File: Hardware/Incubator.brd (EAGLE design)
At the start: 50 x 50 mm, 41 parts, among them IC1 STM32F050F, IC2 LD117AS33TR, IC3 7805DT, Q1 8 MHz, Q2 BC817-16LT1SMD, U1 LCD-16X28X2, X1 22-23-2051, X2 22-23-2041, X3 22-23-2021, X4 22-23-2021

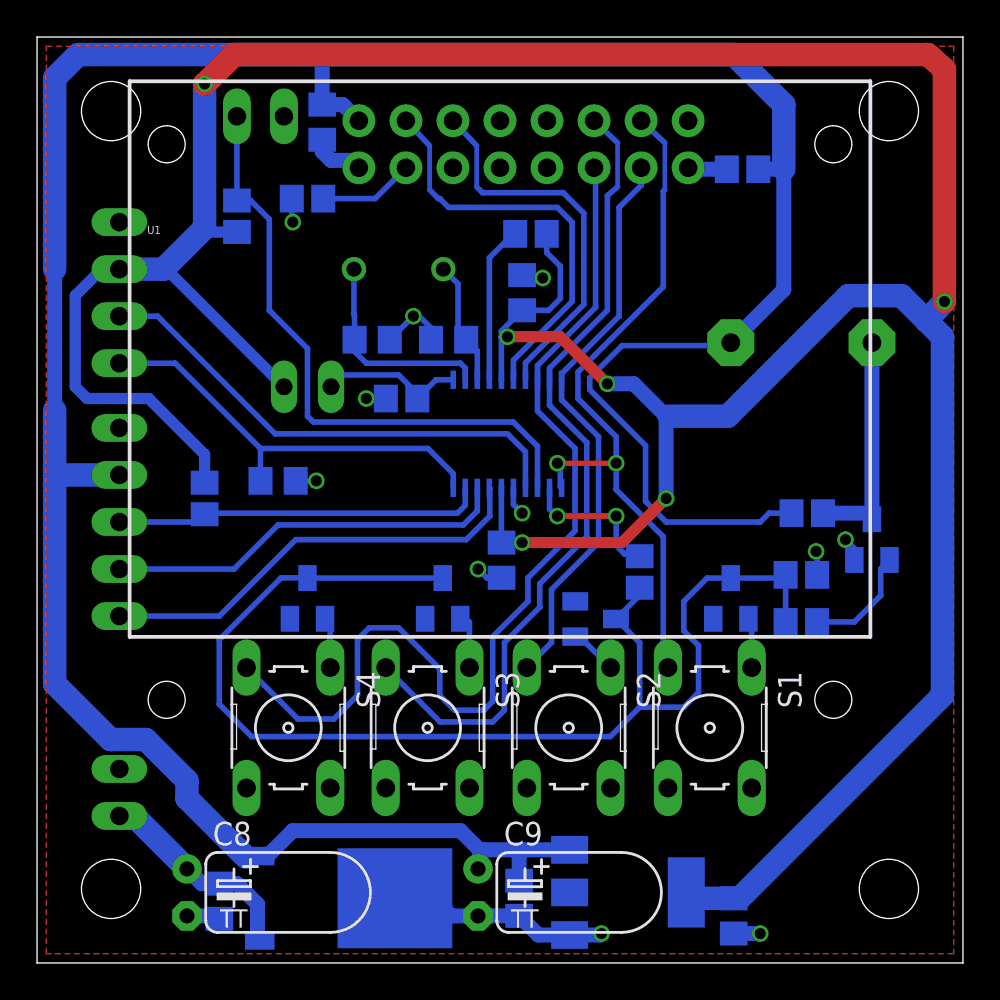
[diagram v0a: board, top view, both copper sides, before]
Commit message: Release version
Version for production
- 3 buttons on control board
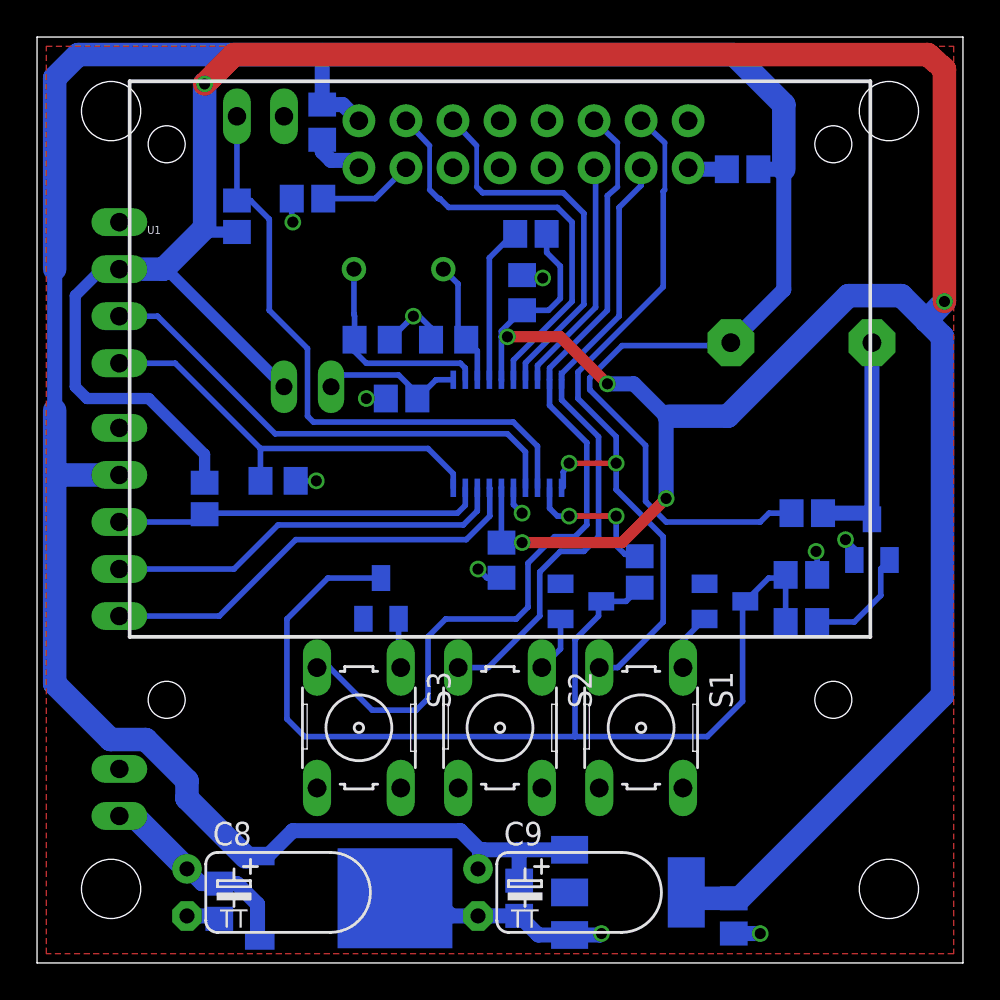
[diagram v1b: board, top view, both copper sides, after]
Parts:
- removed D4: BAV99, diode:SOT23
- removed S4: (no value), switch-omron:B3F-10XX
- R4: value 100 -> 200
- moved S1 3.71 mm to (32.6, 12.7)
- moved S2 3.71 mm to (25.0, 12.7)
- moved S3 3.71 mm to (17.4, 12.7)
- moved D3 3.33 mm to (18.6, 19.7)
- moved D2 1.24 mm to (29.4, 19.5)
- moved D1 0.35 mm to (37.1, 19.5), turned to 90 degrees
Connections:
- removed net N$20: D4.1, S4.1
- net N$11: no longer S4.3
- net N$16: no longer D4.3
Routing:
- net N$11: track 54.0 -> 12.8 mm
- net N$16: track 65.9 -> 58.9 mm
- net N$12: track 44.5 -> 47.8 mm
- net N$13: track 31.2 -> 34.4 mm
- net N$20: track 2.75 -> 0.00 mm
- net N$14: track 38.6 -> 40.0 mm
